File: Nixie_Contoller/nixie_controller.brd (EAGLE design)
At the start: 113 x 51.7 mm, 46 parts, among them IC1 DS1307, IC2 MAX1771ESA, IC4 MPM3630GQV-P, J1 CON-SOCJ-2155, Q1 16MHz, T1 IRF644PBF, U1 328P, U2 HU2032-LF, Y2 32.768kHz

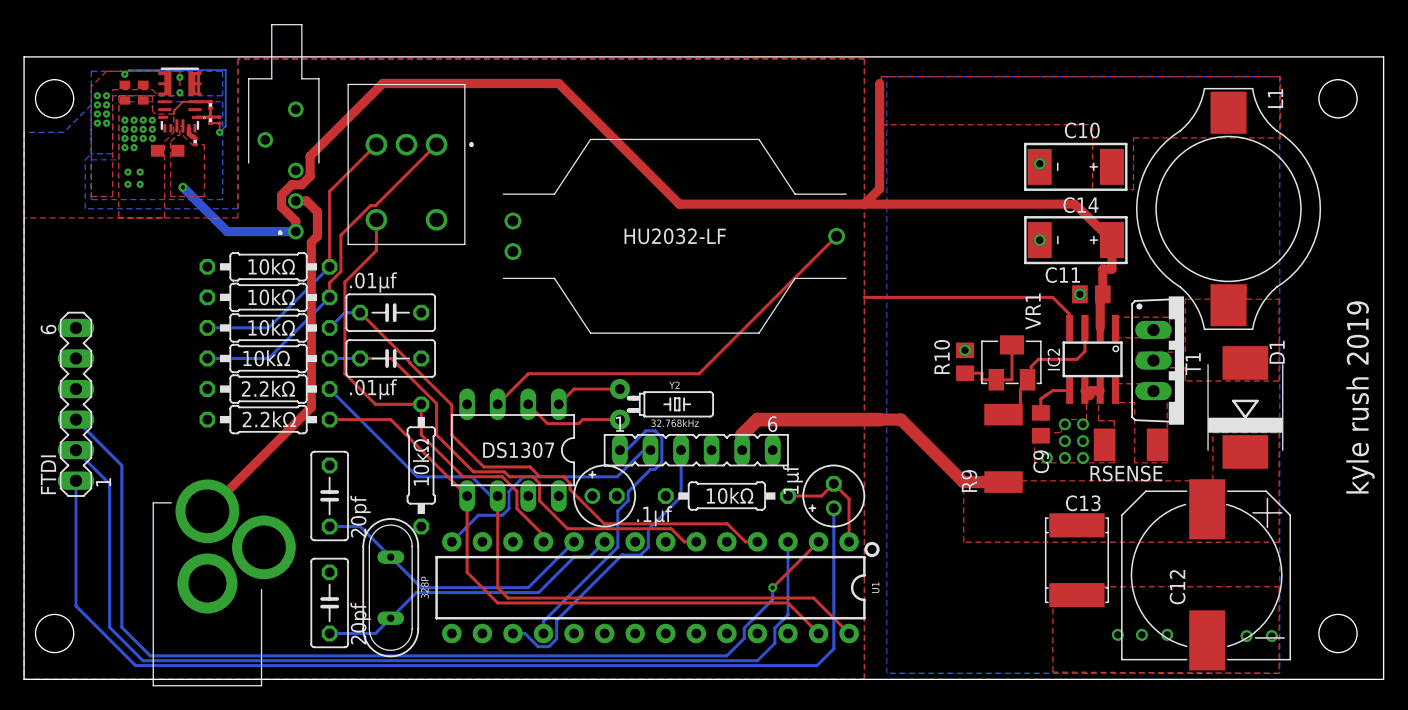
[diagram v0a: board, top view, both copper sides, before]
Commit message: Revert "Adds LV switching PSU"
This reverts commit 12f529c285d7cae732b9ac692bbbf0adcfd9615d.
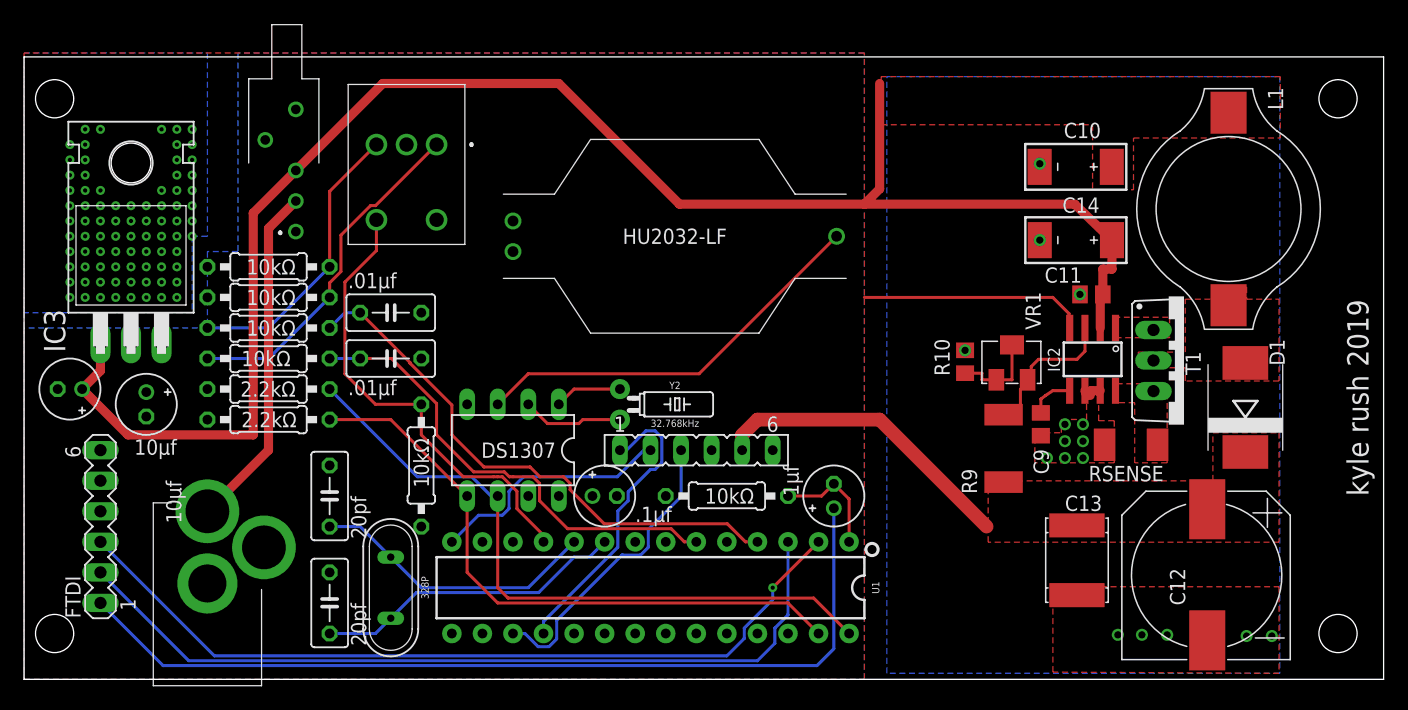
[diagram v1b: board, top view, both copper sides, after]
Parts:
- removed C16, C17: 22pf, rcl:C0402
- removed IC4: MPM3630GQV-P, SamacSys_Parts:QFN-20(3MMX5MMX1.6MM)
- removed R11: 6.98k, rcl:R0201
- removed R12: 51k, rcl:R0201
- removed R14: 100k, rcl:R0201
- added IC3: 7805T, linear:TO220H
- C1: value 22pf -> 10μf; device rcl:C0201 -> rcl:E2-5
- C2: value 22pf -> 10μf; device rcl:C0603 -> rcl:E2-5
- moved C1 25.6 mm to (3.81, 22.9), turned to 180 degrees
- moved C2 21.2 mm to (10.2, 21.6), turned to 270 degrees
- moved FTDI 10.4 mm to (6.35, 11.4)
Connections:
- removed net N$25: IC4.4, IC4.5, IC4.6
- removed net N$28: IC4.17, R14.2
- removed net N$31: C1.2, IC4.1, R11.2, R12.2
- net +12V: now also C1.+, IC3.1, S2.3; no longer C2.1, IC4.16, R14.1, S2.1
- net GND: now also C1.-, C2.-, IC3.2; no longer C16.2, C17.2, C2.2, IC4.12, IC4.13, IC4.14, IC4.3, R11.1
- net VCC: now also C2.+, IC3.3; no longer C1.1, C16.1, C17.1, IC4.7, IC4.8, IC4.9, R12.1
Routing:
- net +12V: track 112.5 -> 140.0 mm, vias 1 -> 0
- net VCC: track 15.5 -> 0.00 mm, vias 12 -> 0
- net N$22: track 82.8 -> 68.6 mm
- net N$21: track 81.8 -> 68.6 mm
- net N$17: track 87.7 -> 75.4 mm
- net GND: track 24.0 -> 20.4 mm, vias 33 -> 97
- net N$31: track 2.68 -> 0.00 mm
- net N$6: track 30.8 -> 28.8 mm
- net N$25: track 1.70 -> 0.00 mm
- net N$28: track 1.14 -> 0.00 mm
- net N$18: track 25.2 -> 26.0 mm
- removed copper zone on layer 1, net VCC

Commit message: Adds LV switching PSU
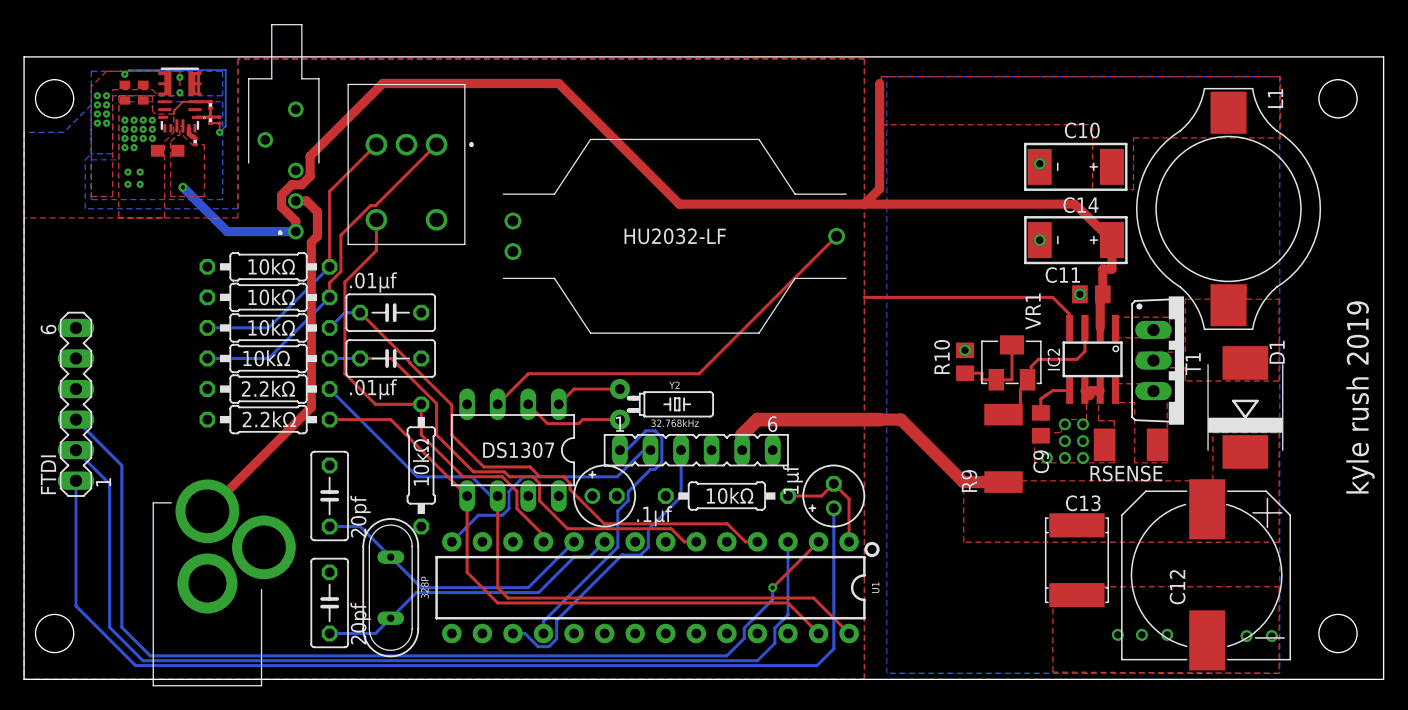
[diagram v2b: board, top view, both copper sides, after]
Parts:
- removed IC3: 7805T, linear:TO220H
- added C16, C17: 22pf, rcl:C0402
- added IC4: MPM3630GQV-P, SamacSys_Parts:QFN-20(3MMX5MMX1.6MM)
- added R11: 6.98k, rcl:R0201
- added R12: 51k, rcl:R0201
- added R14: 100k, rcl:R0201
- C1: value 10μf -> 22pf; device rcl:E2-5 -> rcl:C0201
- C2: value 10μf -> 22pf; device rcl:E2-5 -> rcl:C0603
- moved C1 25.6 mm to (16.3, 45.2), turned to 90 degrees
- moved C2 21.2 mm to (11.9, 42.7), turned to 180 degrees
- moved FTDI 10.4 mm to (4.32, 21.6)
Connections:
- new net N$25: IC4.4, IC4.5, IC4.6
- new net N$28: IC4.17, R14.2
- new net N$31: C1.2, IC4.1, R11.2, R12.2
- net +12V: now also C2.1, IC4.16, R14.1, S2.1; no longer C1.+, IC3.1, S2.3
- net GND: now also C16.2, C17.2, C2.2, IC4.12, IC4.13, IC4.14, IC4.3, R11.1; no longer C1.-, C2.-, IC3.2
- net VCC: now also C1.1, C16.1, C17.1, IC4.7, IC4.8, IC4.9, R12.1; no longer C2.+, IC3.3
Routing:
- net +12V: track 140.0 -> 112.5 mm, vias 0 -> 1
- net VCC: track 0.00 -> 15.5 mm, vias 0 -> 12
- net N$22: track 68.6 -> 82.8 mm
- net N$21: track 68.6 -> 81.8 mm
- net N$17: track 75.4 -> 87.7 mm
- net GND: track 20.4 -> 24.0 mm, vias 97 -> 33
- net N$31: track 0.00 -> 2.68 mm
- net N$6: track 28.8 -> 30.8 mm
- net N$25: track 0.00 -> 1.70 mm
- net N$28: track 0.00 -> 1.14 mm
- net N$18: track 26.0 -> 25.2 mm
- added copper zone on layer 1, net VCC
